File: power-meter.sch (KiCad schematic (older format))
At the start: 27 parts, among them P1101 CONN_01X02, P1102 CONN_01X02, U1101 ADL5513, U1102 REG101NA-5, X1101 SMA, X1102 SMB, X1103 SMB

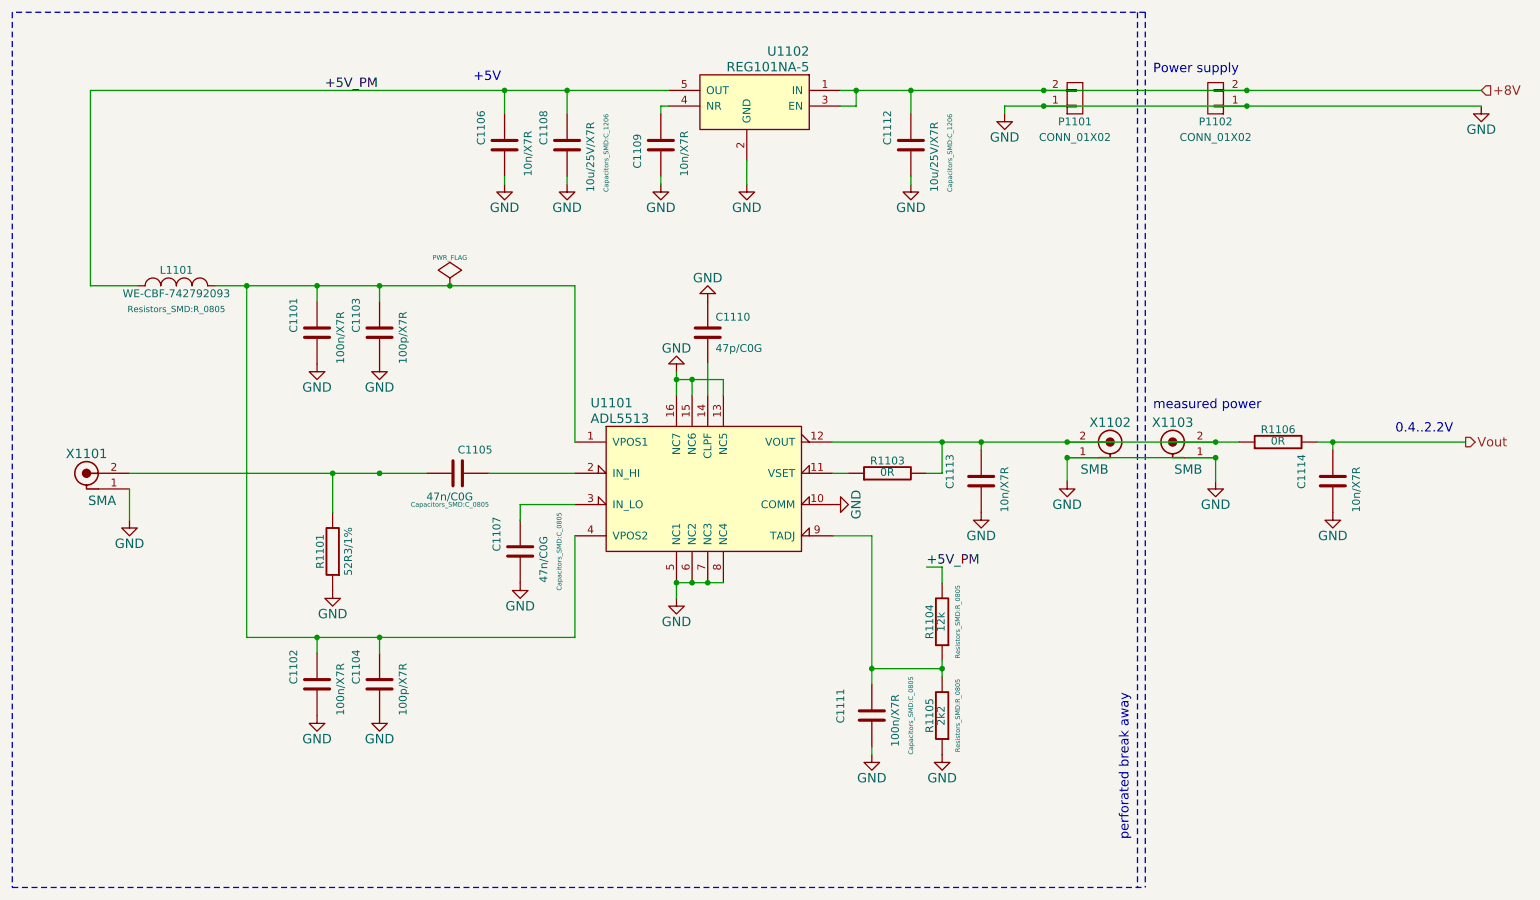
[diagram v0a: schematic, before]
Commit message: fixed missing Rs before Potis - fixed (removed) AD7294 Vpp connection
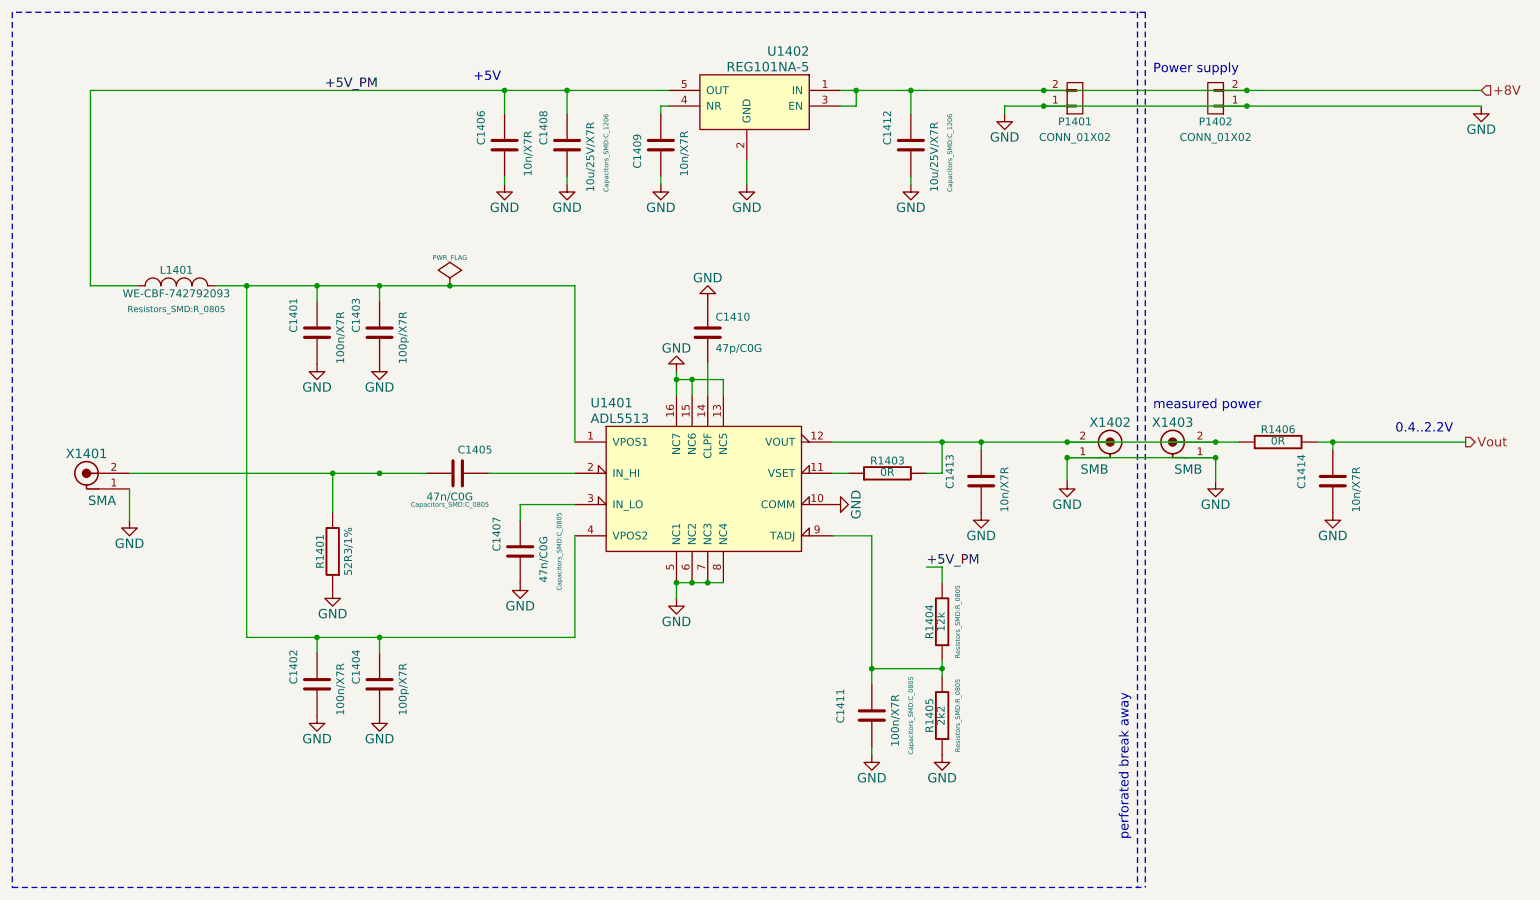
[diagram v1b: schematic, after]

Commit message: RevC
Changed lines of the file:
@@
 LIBS:EtherDue_peripherals-cache
 LIBS:EtherDue_Power-cache
-LIBS:power
-LIBS:device
-LIBS:transistors
-LIBS:conn
-LIBS:linear
-LIBS:regul
-LIBS:74xx
-LIBS:cmos4000
-LIBS:adc-dac
-LIBS:memory
-LIBS:xilinx
-LIBS:microcontrollers
-LIBS:dsp
-LIBS:microchip
-LIBS:analog_switches
-LIBS:motorola
-LIBS:texas
-LIBS:intel
-LIBS:audio
-LIBS:interface
-LIBS:digital-audio
-LIBS:philips
-LIBS:display
-LIBS:cypress
-LIBS:siliconi
-LIBS:opto
-LIBS:atmel
-LIBS:contrib
-LIBS:valves
 LIBS:zeilhofer
 LIBS:w_transistor
@@
 AR Path="/5501D628/553D9FA6" Ref="U1401"  Part="1"
 AR Path="/553D9FA6" Ref="U1401"  Part="1"
-F 0 "U1201" H 4800 4250 60  0000 L CNN
+F 0 "U1401" H 4800 4250 60  0000 L CNN
 F 1 "ADL5513" H 4800 4150 60  0000 L CNN
 F 2 "zeilhofer:LFCSP16" H 5250 4250 60  0001 C CNN
@@
 AR Path="/5501D2B0/553D9FEE" Ref="R1303"  Part="1"
 AR Path="/5501D628/553D9FEE" Ref="R1403"  Part="1"
-F 0 "R1203" V 6780 3700 50  0000 C CNN
+F 0 "R1403" V 6780 3700 50  0000 C CNN
 F 1 "0R" V 6707 3701 50  0000 C CNN
 F 2 "Resistors_SMD:R_0603" V 6630 3700 30  0001 C CNN
@@
 AR Path="/5501D2B0/553DA101" Ref="X1302"  Part="1"
 AR Path="/5501D628/553DA101" Ref="X1402"  Part="1"
-F 0 "X1202" H 7575 3625 60  0000 C CNN
+F 0 "X1402" H 7575 3625 60  0000 C CNN
 F 1 "SMB" H 7675 3325 60  0000 C CNN
 F 2 "zeilhofer:SMB-RS#420-5401_wirepad" H 7650 3900 60  0001 C CNN
@@
 AR Path="/5501D2B0/553DA231" Ref="X1303"  Part="1"
 AR Path="/5501D628/553DA231" Ref="X1403"  Part="1"
-F 0 "X1203" H 8525 3625 60  0000 C CNN
+F 0 "X1403" H 8525 3625 60  0000 C CNN
 F 1 "SMB" H 8625 3325 60  0000 C CNN
 F 2 "zeilhofer:SMB-RS#420-5401_wirepad" H 8600 3900 60  0001 C CNN
@@
 AR Path="/5501D2B0/553DA62F" Ref="R1306"  Part="1"
 AR Path="/5501D628/553DA62F" Ref="R1406"  Part="1"
-F 0 "R1206" V 9280 3500 50  0000 C CNN
+F 0 "R1406" V 9280 3500 50  0000 C CNN
 F 1 "0R" V 9207 3501 50  0000 C CNN
 F 2 "Resistors_SMD:R_0603" V 9130 3500 30  0001 C CNN
@@
 AR Path="/5501D2B0/553DA6E9" Ref="C1314"  Part="1"
 AR Path="/5501D628/553DA6E9" Ref="C1414"  Part="1"
-F 0 "C1214" V 9750 3700 50  0000 L CNN
+F 0 "C1414" V 9750 3700 50  0000 L CNN
 F 1 "10n/X7R" V 9400 3550 50  0000 L CNN
 F 2 "Capacitors_SMD:C_0603" H 9588 3600 30  0001 C CNN
@@
 AR Path="/5501D2B0/553DAF62" Ref="P1301"  Part="1"
 AR Path="/5501D628/553DAF62" Ref="P1401"  Part="1"
-F 0 "P1201" H 7900 1450 50  0000 C CNN
+F 0 "P1401" H 7900 1450 50  0000 C CNN
 F 1 "CONN_01X02" H 7900 1550 50  0000 C CNN
 F 2 "Pin_Headers:Pin_Header_Straight_1x02" H 7900 1300 60  0001 C CNN
@@
 AR Path="/5501D2B0/553DB787" Ref="R1304"  Part="1"
 AR Path="/5501D628/553DB787" Ref="R1404"  Part="1"
-F 0 "R1204" V 7130 4650 50  0000 C CNN
+F 0 "R1404" V 7130 4650 50  0000 C CNN
 F 1 "12k" V 7057 4651 50  0000 C CNN
 F 2 "Resistors_SMD:R_0805" V 6950 4650 30  0000 C CNN
@@
 AR Path="/5501D2B0/553DBB38" Ref="R1305"  Part="1"
 AR Path="/5501D628/553DBB38" Ref="R1405"  Part="1"
-F 0 "R1205" V 7130 5250 50  0000 C CNN
+F 0 "R1405" V 7130 5250 50  0000 C CNN
 F 1 "2k2" V 7057 5251 50  0000 C CNN
 F 2 "Resistors_SMD:R_0805" V 6950 5250 30  0000 C CNN
@@
 AR Path="/5501D2B0/553DC738" Ref="C1310"  Part="1"
 AR Path="/5501D628/553DC738" Ref="C1410"  Part="1"
-F 0 "C1210" H 5600 2900 50  0000 L CNN
+F 0 "C1410" H 5600 2900 50  0000 L CNN
 F 1 "47p/C0G" H 5600 2700 50  0000 L CNN
 F 2 "Capacitors_SMD:C_0603" H 5588 2650 30  0001 C CNN
@@
 AR Path="/5501D2B0/553DD8A7" Ref="P1302"  Part="1"
 AR Path="/5501D628/553DD8A7" Ref="P1402"  Part="1"
-F 0 "P1202" H 8800 1450 50  0000 C CNN
+F 0 "P1402" H 8800 1450 50  0000 C CNN
 F 1 "CONN_01X02" H 8800 1550 50  0000 C CNN
 F 2 "Pin_Headers:Pin_Header_Straight_1x02" H 8800 1300 60  0001 C CNN
@@
 AR Path="/5501D2B0/553E1B3F" Ref="U1302"  Part="1"
 AR Path="/5501D628/553E1B3F" Ref="U1402"  Part="1"
-F 0 "U1202" H 5600 1200 60  0000 L CNN
+F 0 "U1402" H 5600 1200 60  0000 L CNN
 F 1 "REG101NA-5" H 5600 1100 60  0000 L CNN
 F 2 "zeilhofer:DBV(R-PDSO-G5)" H 5900 1100 60  0001 C CNN
@@
 AR Path="/5501D2B0/553E1B4D" Ref="C1309"  Part="1"
 AR Path="/5501D628/553E1B4D" Ref="C1409"  Part="1"
-F 0 "C1209" V 5100 1450 50  0000 L CNN
+F 0 "C1409" V 5100 1450 50  0000 L CNN
 F 1 "10n/X7R" V 5400 1400 50  0000 L CNN
 F 2 "Capacitors_SMD:C_0603" H 5288 1450 30  0001 C CNN
@@
 AR Path="/5501D2B0/553E1B6C" Ref="C1308"  Part="1"
 AR Path="/5501D628/553E1B6C" Ref="C1408"  Part="1"
-F 0 "C1208" V 4500 1600 50  0000 L CNN
+F 0 "C1408" V 4500 1600 50  0000 L CNN
 F 1 "10u/25V/X7R" V 4800 1300 50  0000 L CNN
 F 2 "Capacitors_SMD:C_1206" V 4900 1550 30  0000 C CNN
@@
 AR Path="/5501D2B0/553E1B8B" Ref="C1306"  Part="1"
 AR Path="/5501D628/553E1B8B" Ref="C1406"  Part="1"
-F 0 "C1206" V 4100 1600 50  0000 L CNN
+F 0 "C1406" V 4100 1600 50  0000 L CNN
 F 1 "10n/X7R" V 4400 1400 50  0000 L CNN
 F 2 "Capacitors_SMD:C_0603" H 4288 1450 30  0001 C CNN
@@
 AR Path="/5501D2B0/553E50A5" Ref="C1301"  Part="1"
 AR Path="/5501D628/553E50A5" Ref="C1401"  Part="1"
-F 0 "C1201" V 2900 2800 50  0000 L CNN
+F 0 "C1401" V 2900 2800 50  0000 L CNN
 F 1 "100n/X7R" V 3200 2600 50  0000 L CNN
 F 2 "Capacitors_SMD:C_0603" H 3088 2650 30  0001 C CNN
@@
 AR Path="/5501D2B0/553E53AB" Ref="C1303"  Part="1"
 AR Path="/5501D628/553E53AB" Ref="C1403"  Part="1"
-F 0 "C1203" V 3300 2800 50  0000 L CNN
+F 0 "C1403" V 3300 2800 50  0000 L CNN
 F 1 "100p/X7R" V 3600 2600 50  0000 L CNN
 F 2 "Capacitors_SMD:C_0603" H 3488 2650 30  0001 C CNN
@@
 AR Path="/5501D2B0/553E5599" Ref="L1301"  Part="1"
 AR Path="/5501D628/553E5599" Ref="L1401"  Part="1"
-F 0 "L1201" H 2150 2600 50  0000 C CNN
+F 0 "L1401" H 2150 2600 50  0000 C CNN
 F 1 "WE-CBF-742792093" H 2150 2450 50  0000 C CNN
 F 2 "Resistors_SMD:R_0805" H 2150 2350 40  0000 C CNN
@@
 AR Path="/5501D2B0/553E5E6A" Ref="C1302"  Part="1"
 AR Path="/5501D628/553E5E6A" Ref="C1402"  Part="1"
-F 0 "C1202" V 2900 5050 50  0000 L CNN
+F 0 "C1402" V 2900 5050 50  0000 L CNN
 F 1 "100n/X7R" V 3200 4850 50  0000 L CNN
 F 2 "Capacitors_SMD:C_0603" H 3088 4900 30  0001 C CNN
@@
 AR Path="/5501D2B0/553E5E70" Ref="C1304"  Part="1"
 AR Path="/5501D628/553E5E70" Ref="C1404"  Part="1"
-F 0 "C1204" V 3300 5050 50  0000 L CNN
+F 0 "C1404" V 3300 5050 50  0000 L CNN
 F 1 "100p/X7R" V 3600 4850 50  0000 L CNN
 F 2 "Capacitors_SMD:C_0603" H 3488 4900 30  0001 C CNN
@@
 AR Path="/5501D2B0/553E5F91" Ref="X1301"  Part="1"
 AR Path="/5501D628/553E5F91" Ref="X1401"  Part="1"
-F 0 "X1201" H 1575 3825 60  0000 C CNN
+F 0 "X1401" H 1575 3825 60  0000 C CNN
 F 1 "SMA" H 1675 3525 60  0000 C CNN
 F 2 "zeilhofer:SMA-RS#616-3422" H 1650 4100 60  0001 C CNN
@@
 AR Path="/5501D2B0/553E613A" Ref="C1305"  Part="1"
 AR Path="/5501D628/553E613A" Ref="C1405"  Part="1"
-F 0 "C1205" V 3800 3700 50  0000 L CNN
+F 0 "C1405" V 3800 3700 50  0000 L CNN
 F 1 "47n/C0G" V 4100 3500 50  0000 L CNN
 F 2 "Capacitors_SMD:C_0805" V 4150 3650 30  0000 C CNN
@@
 AR Path="/5501D2B0/553E829A" Ref="C1307"  Part="1"
 AR Path="/5501D628/553E829A" Ref="C1407"  Part="1"
-F 0 "C1207" V 4200 4200 50  0000 L CNN
+F 0 "C1407" V 4200 4200 50  0000 L CNN
 F 1 "47n/C0G" V 4500 4000 50  0000 L CNN
 F 2 "Capacitors_SMD:C_0805" V 4600 4200 30  0000 C CNN
@@
 AR Path="/5501D2B0/5540C488" Ref="C1313"  Part="1"
 AR Path="/5501D628/5540C488" Ref="C1413"  Part="1"
-F 0 "C1213" V 7500 3700 50  0000 L CNN
+F 0 "C1413" V 7500 3700 50  0000 L CNN
 F 1 "10n/X7R" V 7150 3550 50  0000 L CNN
 F 2 "Capacitors_SMD:C_0603" H 7338 3600 30  0001 C CNN
@@
 AR Path="/5501D2B0/5540C544" Ref="C1311"  Part="1"
 AR Path="/5501D628/5540C544" Ref="C1411"  Part="1"
-F 0 "C1211" V 6800 5200 50  0000 L CNN
+F 0 "C1411" V 6800 5200 50  0000 L CNN
 F 1 "100n/X7R" V 6450 5050 50  0000 L CNN
 F 2 "Capacitors_SMD:C_0805" V 6350 5250 30  0000 C CNN
@@
 AR Path="/5501D2B0/54FD7889" Ref="C1312"  Part="1"
 AR Path="/5501D628/54FD7889" Ref="C1412"  Part="1"
-F 0 "C1212" V 6700 1600 50  0000 L CNN
+F 0 "C1412" V 6700 1600 50  0000 L CNN
 F 1 "10u/25V/X7R" V 7000 1300 50  0000 L CNN
 F 2 "Capacitors_SMD:C_1206" V 7100 1550 30  0000 C CNN
@@
 AR Path="/5501D2B0/54FFF0ED" Ref="R1301"  Part="1"
 AR Path="/5501D628/54FFF0ED" Ref="R1401"  Part="1"
-F 0 "R1201" V 3230 4200 50  0000 C CNN
+F 0 "R1401" V 3230 4200 50  0000 C CNN
 F 1 "52R3/1%" V 3050 4200 50  0000 C CNN
 F 2 "Resistors_SMD:R_0805" V 3080 4200 30  0001 C CNN
